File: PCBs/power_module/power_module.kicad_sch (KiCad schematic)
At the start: 28 parts, among them J10 mlx_2pin, J11 Conn_02x07_Odd_Even, J12 Conn_02x08_Odd_Even, J14 mlx_4pin, J2 SM03B-GHS-TB, J3 Conn_02x08_Odd_Even, J7 SM07B-GHS-TB, J8 B7B-XH-A, J9 SM08B-GHS-TB, U1 SN74LVC1T45DBV

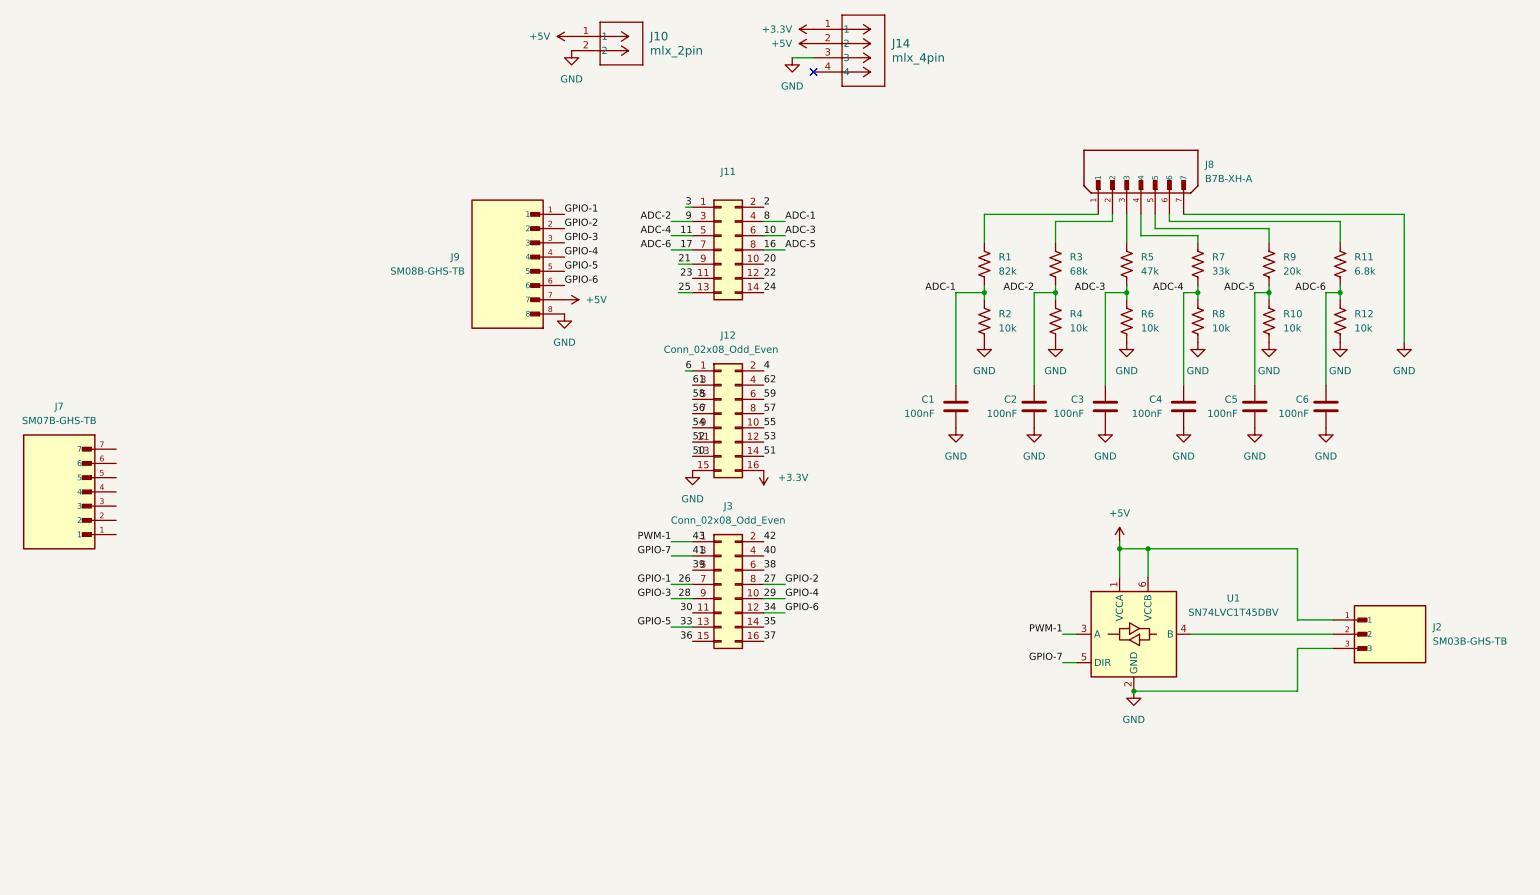
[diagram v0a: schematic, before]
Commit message: finished draft of power_module, ready for review
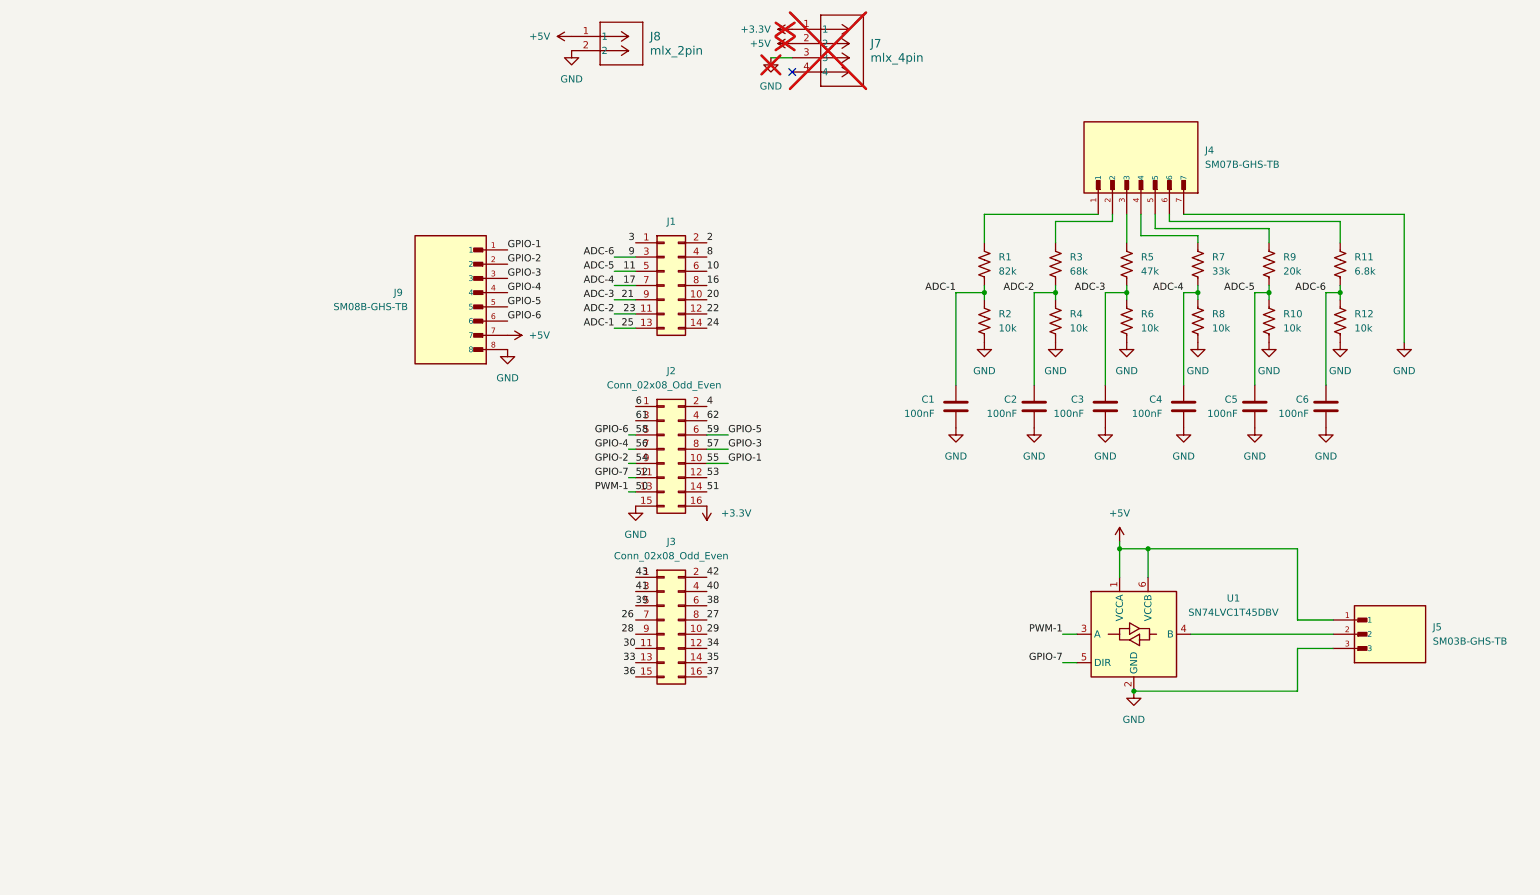
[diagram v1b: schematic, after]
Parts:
- removed J11: Conn_02x07_Odd_Even, Connector_PinHeader_2.54mm:PinHeader_2x07_P2.54mm_Vertical, symbol Connector_Generic:Conn_02x07_Odd_Even
- removed J12: Conn_02x08_Odd_Even, Connector_PinHeader_2.54mm:PinHeader_2x08_P2.54mm_Vertical, symbol Connector_Generic:Conn_02x08_Odd_Even
- removed J14: mlx_4pin, CONN_SD-43045-004_04_MOL, symbol 0430450409_mlx_4pin:430450409
- removed J7: SM07B-GHS-TB, SM07B-GHS-TB:JST_SM07B-GHS-TB, symbol SM07B-GHS-TB:SM07B-GHS-TB
- removed J8: B7B-XH-A, B7B-XH-A:JST_B7B-XH-A, symbol B7B-XH-A:B7B-XH-A
- added J1: Conn_02x07_Odd_Even, Connector_PinHeader_2.54mm:PinHeader_2x07_P2.54mm_Vertical, symbol Connector_Generic:Conn_02x07_Odd_Even
- added J2: Conn_02x08_Odd_Even, Connector_PinHeader_2.54mm:PinHeader_2x08_P2.54mm_Vertical, symbol Connector_Generic:Conn_02x08_Odd_Even
- added J4: SM07B-GHS-TB, Connector_JST:JST_GH_SM07B-GHS-TB_1x07-1MP_P1.25mm_Horizontal, symbol SM07B-GHS-TB:SM07B-GHS-TB
- added J7: mlx_4pin, CONN_SD-43045-001_04_MOL, symbol 430450400_mlx_4pin:430450400
- C1, C2, C3, C4, C5, C6: footprint (none) -> Capacitor_SMD:C_0805_2012Metric_Pad1.18x1.45mm_HandSolder
- J5: renamed from J2; footprint SM03B-GHS-TB:JST_SM03B-GHS-TB -> Connector_JST:JST_GH_SM03B-GHS-TB_1x03-1MP_P1.25mm_Horizontal
- J8: renamed from J10; footprint CONN_SD-43045-001_02_MOL -> Connector_Molex:Molex_Micro-Fit_3.0_43045-0200_2x01_P3.00mm_Horizontal
- J9: footprint SM08B-GHS-TB:JST_SM08B-GHS-TB -> Connector_JST:JST_GH_SM08B-GHS-TB_1x08-1MP_P1.25mm_Horizontal
- R1, R10, R11, R12, R2, R3, R4, R5, R6, R7, R8, R9: footprint (none) -> Resistor_SMD:R_0805_2012Metric_Pad1.20x1.40mm_HandSolder
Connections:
- net +3.3V: now also J2.16 (Pin_16), J7.1
- net +5V: now also J7.2
- net 10: now also J1.6 (Pin_6); no longer C3.1, R5.2, R6.1
- net 11: now also C5.1, R10.1, R9.2, J1.5 (Pin_5); no longer C4.1, R7.2, R8.1
- net 16: now also J1.8 (Pin_8); no longer C5.1, R10.1, R9.2
- net 17: now also C4.1, R7.2, R8.1, J1.7 (Pin_7); no longer C6.1, R11.2, R12.1
- net 2: now also J1.2 (Pin_2)
- net 20: now also J1.10 (Pin_10)
- net 21: now also C3.1, R5.2, R6.1, J1.9 (Pin_9)
- net 22: now also J1.12 (Pin_12)
- net 23: now also C2.1, R3.2, R4.1, J1.11 (Pin_11)
- net 24: now also J1.14 (Pin_14)
- net 25: now also C1.1, R1.2, R2.1, J1.13 (Pin_13)
- net 26: no longer J3.7 (Pin_7), J9.1
- net 27: no longer J9.2
- net 28: no longer J3.9 (Pin_9), J9.3
- net 29: no longer J9.4
- net 33: no longer J9.5
- net 34: no longer J9.6
- net 4: now also J2.2 (Pin_2)
- net 41: no longer U1.5 (DIR)
- net 43: no longer U1.3 (A)
- net 50: now also U1.3 (A), J2.13 (Pin_13)
- net 51: now also J2.14 (Pin_14)
- net 52: now also U1.5 (DIR), J2.11 (Pin_11)
- net 53: now also J2.12 (Pin_12)
- net 54: now also J9.2, J2.9 (Pin_9)
- net 55: now also J9.1, J2.10 (Pin_10)
- net 56: now also J9.4, J2.7 (Pin_7)
- net 57: now also J9.3, J2.8 (Pin_8)
- net 58: now also J9.6, J2.5 (Pin_5)
- net 59: now also J9.5, J2.6 (Pin_6)
- net 6: now also J2.1 (Pin_1)
- net 61: now also J2.3 (Pin_3)
- net 62: now also J2.4 (Pin_4)
- net 8: now also J1.4 (Pin_4); no longer C1.1, R1.2, R2.1
- net 9: now also C6.1, R11.2, R12.1, J1.3 (Pin_3); no longer C2.1, R3.2, R4.1
- net GND: now also J2.15 (Pin_15), J4.7, J7.3
- net at R3.1: now also J4.2
- net at R1.1: now also J4.1
- net at R5.1: now also J4.3
- net at R7.1: now also J4.4
- net at R9.1: now also J4.5
- net at R11.1: now also J4.6

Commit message: first revision
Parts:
- added C7: 10uF, Capacitor_SMD:C_0805_2012Metric_Pad1.18x1.45mm_HandSolder, symbol Device:C
- added C8, C9: 100nF, Capacitor_SMD:C_0805_2012Metric_Pad1.18x1.45mm_HandSolder, symbol Device:C
- added R13: 10k, Resistor_SMD:R_0805_2012Metric_Pad1.20x1.40mm_HandSolder, symbol Device:R_US
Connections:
- net +3.3V: now also U1.1 (VCCA), C8.1
- net +5V: now also C7.1, C9.1; no longer U1.1 (VCCA)
- net 52: no longer U1.5 (DIR)
- net GND: now also C7.2, C8.2, C9.2
- new net: R13.2, U1.5 (DIR)

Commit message: revision 2: added c & r for snl, changed VccA to 3.3v
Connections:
- net 52: now also R13.1
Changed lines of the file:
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@@
+	(wire
+		(pts
+			(xy 146.05 130.81) (xy 147.32 130.81)
+		)
+		(stroke
+			(width 0)
+			(type default)
+		)
+	)
 	(wire
 		(pts

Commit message: 3rd revision: corrected mounting holes
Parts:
- added H1, H2, H3, H4: MountingHole, MountingHole:MountingHole_3.2mm_M3, symbol Mechanical:MountingHole

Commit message: revision 4: shrunk board
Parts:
- removed H3, H4: MountingHole, MountingHole:MountingHole_3.2mm_M3, symbol Mechanical:MountingHole
- removed J7: mlx_4pin, CONN_SD-43045-001_04_MOL, symbol 430450400_mlx_4pin:430450400
- removed J8: mlx_2pin, Connector_Molex:Molex_Micro-Fit_3.0_43045-0200_2x01_P3.00mm_Horizontal, symbol 0430450200_mlx_2pin:430450200
- added J6: SM02B-GHS-TB, SM02B_GHS:JST_SM02B-GHS-TB, symbol SM02B-GHS-TB:SM02B-GHS-TB
- renumbered J9 to J7
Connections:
- net +5V: now also J6.1
- net GND: now also J6.2
- no-connect marks 1 -> 0
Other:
- moved on the sheet: H1, H2

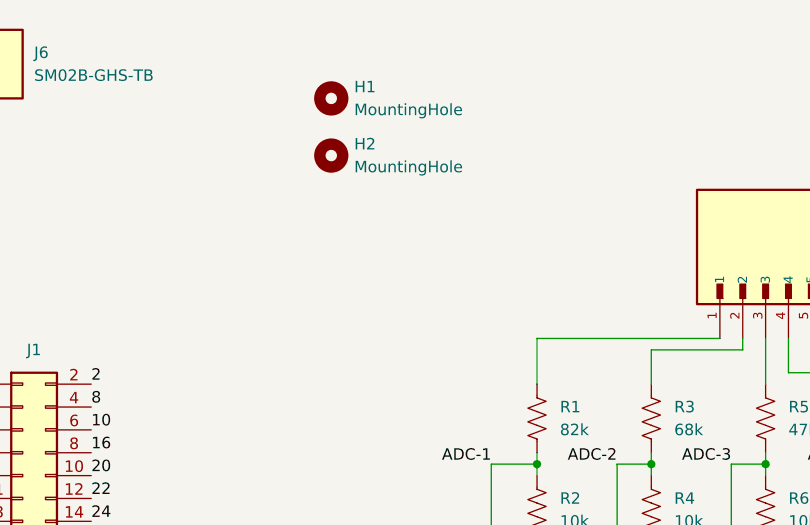
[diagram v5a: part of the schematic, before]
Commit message: revision 5: added mounting holes
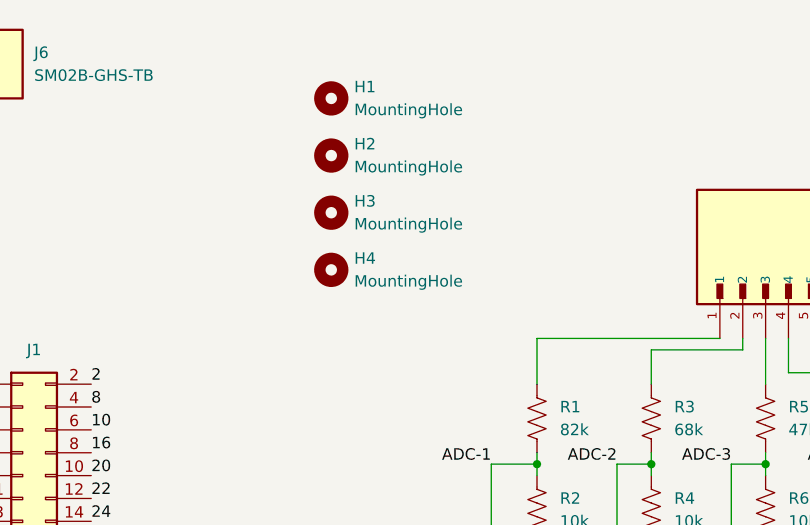
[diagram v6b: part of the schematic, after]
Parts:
- added H3, H4: MountingHole, MountingHole:MountingHole_3.2mm_M3, symbol Mechanical:MountingHole
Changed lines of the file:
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@@
+	)
+	(symbol
+		(lib_id "Mechanical:MountingHole")
+		(at 118.11 36.83 0)
+		(unit 1)
+		(exclude_from_sim no)
+		(in_bom no)
+		(on_board yes)
+		(dnp no)
+		(fields_autoplaced yes)
+		(property "Reference" "H3"
+			(at 120.65 35.5599 0)
+			(effects
+				(font
+					(size 1.27 1.27)
+				)
+				(justify left)
+			)
+		)
+		(property "Value" "MountingHole"
+			(at 120.65 38.0999 0)
+			(effects
+				(font
+					(size 1.27 1.27)
+				)
+				(justify left)
+			)
+		)
+		(property "Footprint" "MountingHole:MountingHole_3.2mm_M3"
+			(at 118.11 36.83 0)
+			(effects
+				(font
+					(size 1.27 1.27)
+				)
+				(hide yes)
+			)
+		)
+		(property "Datasheet" "~"
+			(at 118.11 36.83 0)
+			(effects
+				(font
+					(size 1.27 1.27)
+				)
+				(hide yes)
+			)
+		)
+		(property "Description" "Mounting Hole without connection"
+			(at 118.11 36.83 0)
+			(effects
+				(font
+					(size 1.27 1.27)
+				)
+				(hide yes)
+			)
+		)
+		(instances
+			(project "power_module"
+				(path "/705004fe-9694-4831-a243-8c72357320a8"
+					(reference "H3")
+					(unit 1)
+				)
+			)
+		)
 	)
 	(symbol
@@
 					(unit 1)
 				)
+			)
+		)
+	)
+	(symbol
+		(lib_id "Mechanical:MountingHole")
+		(at 118.11 43.18 0)
+		(unit 1)
+		(exclude_from_sim no)
+		(in_bom no)
+		(on_board yes)
+		(dnp no)
+		(fields_autoplaced yes)
+		(property "Reference" "H4"
+			(at 120.65 41.9099 0)
+			(effects
+				(font
+					(size 1.27 1.27)
+				)
+				(justify left)
+			)
+		)
+		(property "Value" "MountingHole"
+			(at 120.65 44.4499 0)
+			(effects
+				(font
+					(size 1.27 1.27)
+				)
+				(justify left)
+			)
+		)
+		(property "Footprint" "MountingHole:MountingHole_3.2mm_M3"
+			(at 118.11 43.18 0)
+			(effects
+				(font
+					(size 1.27 1.27)
+				)
+				(hide yes)
+			)
+		)
+		(property "Datasheet" "~"
+			(at 118.11 43.18 0)
+			(effects
+				(font
+					(size 1.27 1.27)
+				)
+				(hide yes)
+			)
+		)
+		(property "Description" "Mounting Hole without connection"
+			(at 118.11 43.18 0)
+			(effects
+				(font
+					(size 1.27 1.27)
+				)
+				(hide yes)
+			)
+		)
+		(instances
+			(project "power_module"
+				(path "/705004fe-9694-4831-a243-8c72357320a8"
+					(reference "H4")
+					(unit 1)
+				)
